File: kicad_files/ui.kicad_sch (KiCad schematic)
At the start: 0 parts

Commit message: UI schematic and external connectors
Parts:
- added Q2: NPN, symbol Simulation_SPICE:NPN
- added Q3: NMOS, symbol Simulation_SPICE:NMOS
- added R10, R11, R12: 10k, symbol Device:R_US
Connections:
- new net: Q2.2 (B), Q3.1 (D), R10.2
- new net: Q3.2 (G), R12.1
- new net 5V: R10.1, R11.1
- new net 5V PWM: Q2.3 (E), R11.2
- new net MCU PWM: R12.2
- new net gnd: Q2.1 (C), Q3.3 (S)

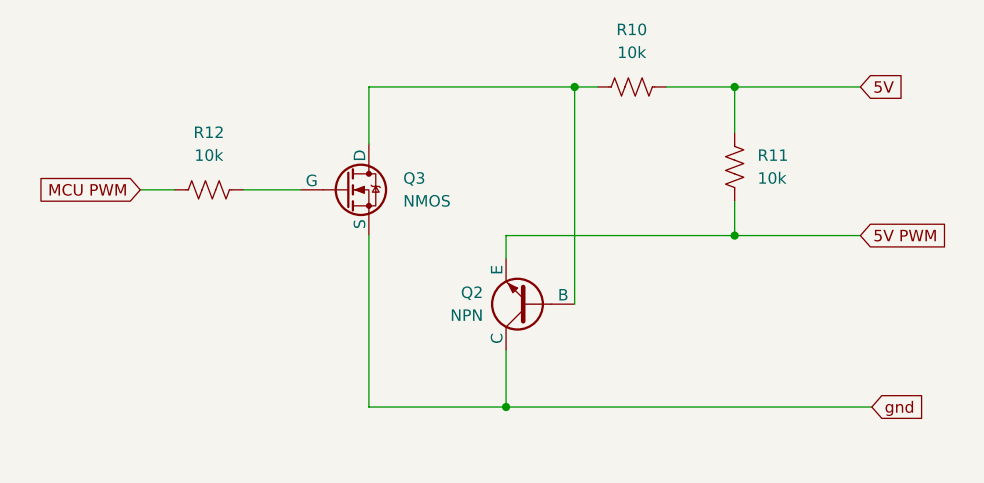
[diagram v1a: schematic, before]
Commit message: Hierarchical labels finished. Flyback diode issue fixed. I2C pins added
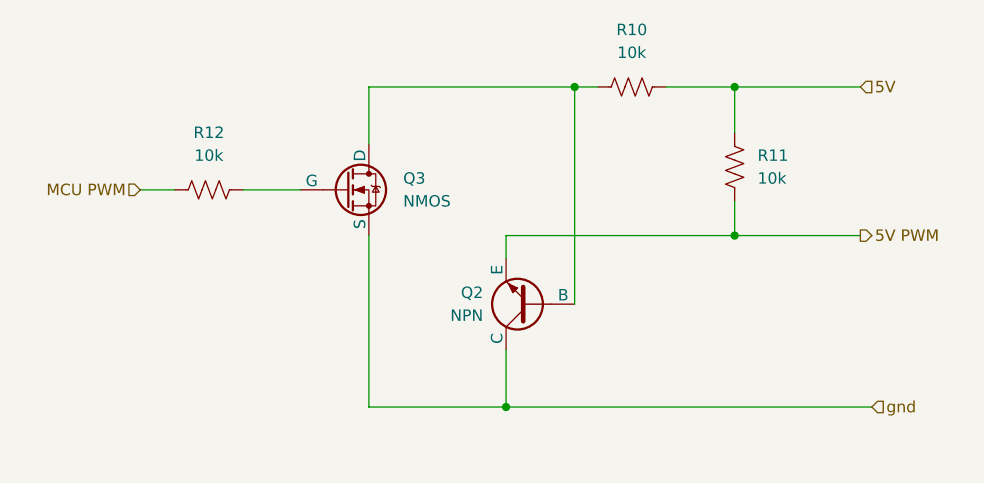
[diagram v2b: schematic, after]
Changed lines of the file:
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@@
 		)
 	)
-	(global_label "5V PWM"
+	(hierarchical_label "gnd"
 		(shape input)
-		(at 177.8 97.79 0)
-		(fields_autoplaced yes)
+		(at 179.07 116.84 0)
 		(effects
 			(font
@@
 			(justify left)
 		)
-		(property "Intersheetrefs" "${INTERSHEET_REFS}"
-			(at 188.2237 97.79 0)
-			(effects
-				(font
-					(size 1.27 1.27)
-				)
-				(justify left)
-				(hide yes)
+	)
+	(hierarchical_label "MCU PWM"
+		(shape input)
+		(at 97.79 92.71 180)
+		(effects
+			(font
+				(size 1.27 1.27)
 			)
+			(justify right)
 		)
 	)
-	(global_label "5V"
-		(shape input)
-		(at 177.8 81.28 0)
-		(fields_autoplaced yes)
+	(hierarchical_label "5V PWM"
+		(shape output)
+		(at 177.8 97.79 0)
 		(effects
 			(font
@@
 			(justify left)
 		)
-		(property "Intersheetrefs" "${INTERSHEET_REFS}"
-			(at 183.0833 81.28 0)
-			(effects
-				(font
-					(size 1.27 1.27)
-				)
-				(justify left)
-				(hide yes)
-			)
-		)
 	)
-	(global_label "MCU PWM"
+	(hierarchical_label "5V"
 		(shape input)
-		(at 97.79 92.71 180)
-		(fields_autoplaced yes)
-		(effects
-			(font
-				(size 1.27 1.27)
-			)
-			(justify right)
-		)
-		(property "Intersheetrefs" "${INTERSHEET_REFS}"
-			(at 85.6125 92.71 0)
-			(effects
-				(font
-					(size 1.27 1.27)
-				)
-				(justify right)
-				(hide yes)
-			)
-		)
-	)
-	(global_label "gnd"
-		(shape input)
-		(at 179.07 116.84 0)
-		(fields_autoplaced yes)
+		(at 177.8 81.28 0)
 		(effects
 			(font
@@
 			(justify left)
 		)
-		(property "Intersheetrefs" "${INTERSHEET_REFS}"
-			(at 185.5022 116.84 0)
-			(effects
-				(font
-					(size 1.27 1.27)
-				)
-				(justify left)
-				(hide yes)
-			)
-		)
 	)

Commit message: ERC errors cleaned. Hierarchical wiring finished. PWM converter change. Motor driver change.
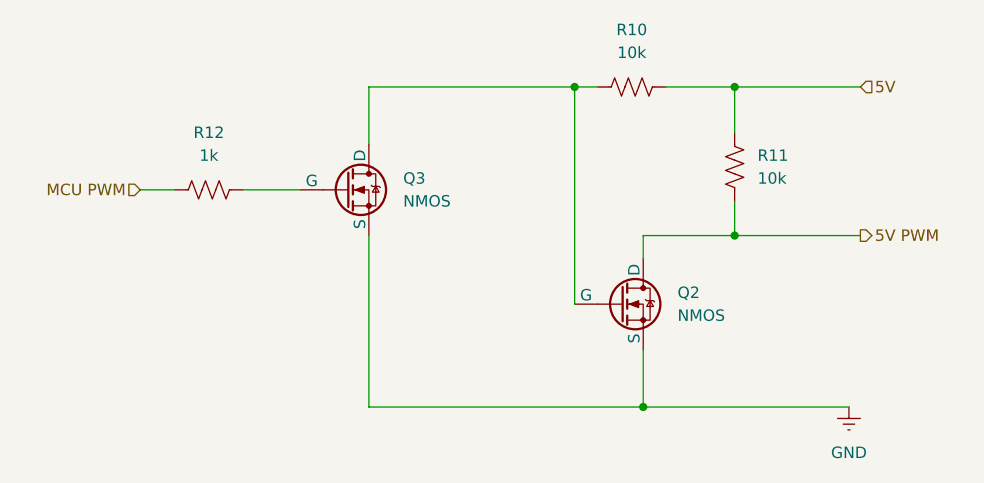
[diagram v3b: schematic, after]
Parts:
- removed Q2: NPN, symbol Simulation_SPICE:NPN
- added Q2: NMOS, symbol Simulation_SPICE:NMOS
- R12: value 10k -> 1k
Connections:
- net 5V PWM: now also Q2.1 (D)
- net at Q3.1 (D), R10.2: now also Q2.2 (G)
- net gnd renamed GND
- net GND: now also Q2.3 (S)
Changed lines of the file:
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@@
 	)
 	(junction
-		(at 138.43 116.84)
+		(at 153.67 116.84)
 		(diameter 0)
 		(color 0 0 0 0)
@@
 	(wire
 		(pts
-			(xy 138.43 110.49) (xy 138.43 116.84)
+			(xy 153.67 110.49) (xy 153.67 116.84)
 		)
 		(stroke
@@
 	(wire
 		(pts
-			(xy 138.43 116.84) (xy 179.07 116.84)
-		)
-		(stroke
-			(width 0)
-			(type default)
-		)
-	)
-	(wire
-		(pts
-			(xy 123.19 116.84) (xy 138.43 116.84)
+			(xy 123.19 116.84) (xy 153.67 116.84)
 		)
 		(stroke
@@
 	(wire
 		(pts
+			(xy 153.67 116.84) (xy 176.53 116.84)
+		)
+		(stroke
+			(width 0)
+			(type default)
+		)
+	)
+	(wire
+		(pts
 			(xy 123.19 81.28) (xy 123.19 87.63)
 		)
@@
 	(wire
 		(pts
-			(xy 138.43 97.79) (xy 138.43 100.33)
+			(xy 153.67 97.79) (xy 153.67 100.33)
 		)
 		(stroke
@@
 	(wire
 		(pts
-			(xy 163.83 97.79) (xy 138.43 97.79)
+			(xy 163.83 97.79) (xy 153.67 97.79)
 		)
 		(stroke
@@
 			(width 0)
 			(type default)
-		)
-	)
-	(hierarchical_label "gnd"
-		(shape input)
-		(at 179.07 116.84 0)
-		(effects
-			(font
-				(size 1.27 1.27)
-			)
-			(justify left)
 		)
 	)
@@
 			)
 			(justify left)
+		)
+	)
+	(symbol
+		(lib_id "Simulation_SPICE:NMOS")
+		(at 151.13 105.41 0)
+		(unit 1)
+		(exclude_from_sim no)
+		(in_bom yes)
+		(on_board yes)
+		(dnp no)
+		(fields_autoplaced yes)
+		(property "Reference" "Q2"
+			(at 157.48 104.1399 0)
+			(effects
+				(font
+					(size 1.27 1.27)
+				)
+				(justify left)
+			)
+		)
+		(property "Value" "NMOS"
+			(at 157.48 106.6799 0)
+			(effects
+				(font
+					(size 1.27 1.27)
+				)
+				(justify left)
+			)
+		)
+		(property "Footprint" ""
+			(at 156.21 102.87 0)
+			(effects
+				(font
+					(size 1.27 1.27)
+				)
+				(hide yes)
+			)
+		)
+		(property "Datasheet" "https://ngspice.sourceforge.io/docs/ngspice-html-manual/manual.xhtml#cha_MOSFETs"
+			(at 151.13 118.11 0)
+			(effects
+				(font
+					(size 1.27 1.27)
+				)
+				(hide yes)
+			)
+		)
+		(property "Description" "N-MOSFET transistor, drain/source/gate"
+			(at 151.13 105.41 0)
+			(effects
+				(font
+					(size 1.27 1.27)
+				)
+				(hide yes)
+			)
+		)
+		(property "Sim.Device" "NMOS"
+			(at 151.13 122.555 0)
+			(effects
+				(font
+					(size 1.27 1.27)
+				)
+				(hide yes)
+			)
+		)
+		(property "Sim.Type" "VDMOS"
+			(at 151.13 124.46 0)
+			(effects
+				(font
+					(size 1.27 1.27)
+				)
+				(hide yes)
+			)
+		)
+		(property "Sim.Pins" "1=D 2=G 3=S"
+			(at 151.13 120.65 0)
+			(effects
+				(font
+					(size 1.27 1.27)
+				)
+				(hide yes)
+			)
+		)
+		(pin "2"
+		)
+		(pin "3"
+		)
+		(pin "1"
+		)
+		(instances
+			(project "kicad_files"
+				(path "/67de3bec-6c8a-4e66-9cf7-9a8a92865209/ce830c06-a9b3-40f6-b6fa-b8cd2779ee31"
+					(reference "Q2")
+					(unit 1)
+				)
+			)
+		)
+	)
+	(symbol
+		(lib_id "power:GNDREF")
+		(at 176.53 116.84 0)
+		(unit 1)
+		(exclude_from_sim no)
+		(in_bom yes)
+		(on_board yes)
+		(dnp no)
+		(fields_autoplaced yes)
+		(property "Reference" "#PWR010"
+			(at 176.53 123.19 0)
+			(effects
+				(font
+					(size 1.27 1.27)
+				)
+				(hide yes)
+			)
+		)
+		(property "Value" "GND"
+			(at 176.53 121.92 0)
+			(effects
+				(font
+					(size 1.27 1.27)
+				)
+			)
+		)
+		(property "Footprint" ""
+			(at 176.53 116.84 0)
+			(effects
+				(font
+					(size 1.27 1.27)
+				)
+				(hide yes)
+			)
+		)
+		(property "Datasheet" ""
+			(at 176.53 116.84 0)
+			(effects
+				(font
+					(size 1.27 1.27)
+				)
+				(hide yes)
+			)
+		)
+		(property "Description" "Power symbol creates a global label with name \"GNDREF\" , reference supply ground"
+			(at 176.53 116.84 0)
+			(effects
+				(font
+					(size 1.27 1.27)
+				)
+				(hide yes)
+			)
+		)
+		(pin "1"
+		)
+		(instances
+			(project "kicad_files"
+				(path "/67de3bec-6c8a-4e66-9cf7-9a8a92865209/ce830c06-a9b3-40f6-b6fa-b8cd2779ee31"
+					(reference "#PWR010")
+					(unit 1)
+				)
+			)
 		)
 	)
@@
 			)
 		)
-		(property "Value" "10k"
+		(property "Value" "1k"
 			(at 105.41 88.9 90)
 			(effects
@@
 					(unit 1)
 				)
-			)
-		)
-	)
-	(symbol
-		(lib_id "Simulation_SPICE:NPN")
-		(at 140.97 105.41 180)
-		(unit 1)
-		(exclude_from_sim no)
-		(in_bom yes)
-		(on_board yes)
-		(dnp no)
-		(fields_autoplaced yes)
-		(property "Reference" "Q2"
-			(at 135.89 104.1399 0)
-			(effects
-				(font
-					(size 1.27 1.27)
-				)
-				(justify left)
-			)
-		)
-		(property "Value" "NPN"
-			(at 135.89 106.6799 0)
-			(effects
-				(font
-					(size 1.27 1.27)
-				)
-				(justify left)
-			)
-		)
-		(property "Footprint" ""
-			(at 77.47 105.41 0)
-			(effects
-				(font
-					(size 1.27 1.27)
-				)
-				(hide yes)
-			)
-		)
-		(property "Datasheet" "https://ngspice.sourceforge.io/docs/ngspice-html-manual/manual.xhtml#cha_BJTs"
-			(at 77.47 105.41 0)
-			(effects
-				(font
-					(size 1.27 1.27)
-				)
-				(hide yes)
-			)
-		)
-		(property "Description" "Bipolar transistor symbol for simulation only, substrate tied to the emitter"
-			(at 140.97 105.41 0)
-			(effects
-				(font
-					(size 1.27 1.27)
-				)
-				(hide yes)
-			)
-		)
-		(property "Sim.Device" "NPN"
-			(at 140.97 105.41 0)
-			(effects
-				(font
-					(size 1.27 1.27)
-				)
-				(hide yes)
-			)
-		)
-		(property "Sim.Type" "GUMMELPOON"
-			(at 140.97 105.41 0)
-			(effects
-				(font
-					(size 1.27 1.27)
-				)
-				(hide yes)
-			)
-		)
-		(property "Sim.Pins" "1=C 2=B 3=E"
-			(at 140.97 105.41 0)
-			(effects
-				(font
-					(size 1.27 1.27)
-				)
-				(hide yes)
-			)
-		)
-		(pin "3"
-		)
-		(pin "1"
-		)
-		(pin "2"
-		)
-		(instances
-			(project ""
-				(path "/67de3bec-6c8a-4e66-9cf7-9a8a92865209/ce830c06-a9b3-40f6-b6fa-b8cd2779ee31"
-					(reference "Q2")
-					(unit 1)
-				)

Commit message: Footprint assignment finished
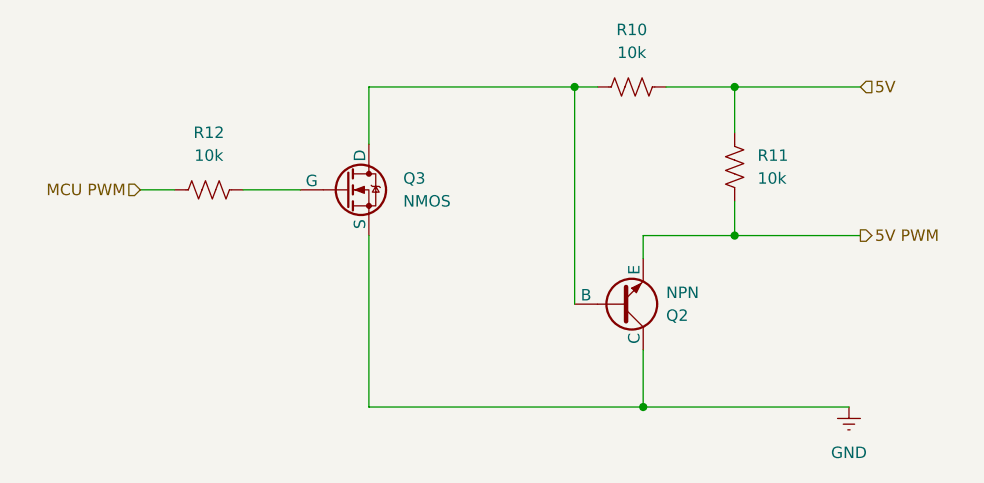
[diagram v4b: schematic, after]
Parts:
- Q2: value NMOS -> NPN; footprint (none) -> Package_TO_SOT_SMD:TSOT-23; symbol Simulation_SPICE:NMOS -> Simulation_SPICE:NPN
- Q3: footprint (none) -> Package_TO_SOT_SMD:SOT-323_SC-70
- R10, R11: footprint (none) -> Resistor_SMD:R_1206_3216Metric_Pad1.30x1.75mm_HandSolder
- R12: value 1k -> 10k; footprint (none) -> Resistor_SMD:R_1206_3216Metric_Pad1.30x1.75mm_HandSolder
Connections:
- net 5V PWM: now also Q2.3 (E); no longer Q2.1 (D)
- net GND: now also Q2.1 (C); no longer Q2.3 (S)
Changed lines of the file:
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@@
 	)
 	(symbol
-		(lib_id "Simulation_SPICE:NMOS")
+		(lib_id "Simulation_SPICE:NPN")
 		(at 151.13 105.41 0)
-		(unit 1)
-		(exclude_from_sim no)
-		(in_bom yes)
-		(on_board yes)
-		(dnp no)
-		(fields_autoplaced yes)
+		(mirror x)
+		(unit 1)
+		(exclude_from_sim no)
+		(in_bom yes)
+		(on_board yes)
+		(dnp no)
 		(property "Reference" "Q2"
-			(at 157.48 104.1399 0)
-			(effects
-				(font
-					(size 1.27 1.27)
-				)
-				(justify left)
-			)
-		)
-		(property "Value" "NMOS"
-			(at 157.48 106.6799 0)
-			(effects
-				(font
-					(size 1.27 1.27)
-				)
-				(justify left)
-			)
-		)
-		(property "Footprint" ""
-			(at 156.21 102.87 0)
-			(effects
-				(font
-					(size 1.27 1.27)
-				)
-				(hide yes)
-			)
-		)
-		(property "Datasheet" "https://ngspice.sourceforge.io/docs/ngspice-html-manual/manual.xhtml#cha_MOSFETs"
-			(at 151.13 118.11 0)
-			(effects
-				(font
-					(size 1.27 1.27)
-				)
-				(hide yes)
-			)
-		)
-		(property "Description" "N-MOSFET transistor, drain/source/gate"
+			(at 156.21 106.6801 0)
+			(effects
+				(font
+					(size 1.27 1.27)
+				)
+				(justify left)
+			)
+		)
+		(property "Value" "NPN"
+			(at 156.21 104.1401 0)
+			(effects
+				(font
+					(size 1.27 1.27)
+				)
+				(justify left)
+			)
+		)
+		(property "Footprint" "Package_TO_SOT_SMD:TSOT-23"
+			(at 214.63 105.41 0)
+			(effects
+				(font
+					(size 1.27 1.27)
+				)
+				(hide yes)
+			)
+		)
+		(property "Datasheet" "https://ngspice.sourceforge.io/docs/ngspice-html-manual/manual.xhtml#cha_BJTs"
+			(at 214.63 105.41 0)
+			(effects
+				(font
+					(size 1.27 1.27)
+				)
+				(hide yes)
+			)
+		)
+		(property "Description" "Bipolar transistor symbol for simulation only, substrate tied to the emitter"
 			(at 151.13 105.41 0)
 			(effects
@@
 			)
 		)
-		(property "Sim.Device" "NMOS"
-			(at 151.13 122.555 0)
-			(effects
-				(font
-					(size 1.27 1.27)
-				)
-				(hide yes)
-			)
-		)
-		(property "Sim.Type" "VDMOS"
-			(at 151.13 124.46 0)
-			(effects
-				(font
-					(size 1.27 1.27)
-				)
-				(hide yes)
-			)
-		)
-		(property "Sim.Pins" "1=D 2=G 3=S"
-			(at 151.13 120.65 0)
+		(property "Sim.Device" "NPN"
+			(at 151.13 105.41 0)
+			(effects
+				(font
+					(size 1.27 1.27)
+				)
+				(hide yes)
+			)
+		)
+		(property "Sim.Type" "GUMMELPOON"
+			(at 151.13 105.41 0)
+			(effects
+				(font
+					(size 1.27 1.27)
+				)
+				(hide yes)
+			)
+		)
+		(property "Sim.Pins" "1=C 2=B 3=E"
+			(at 151.13 105.41 0)
 			(effects
 				(font
@@
 			)
 		)
-		(property "Footprint" ""
+		(property "Footprint" "Resistor_SMD:R_1206_3216Metric_Pad1.30x1.75mm_HandSolder"
 			(at 152.146 82.296 90)
 			(effects
@@
 			)
 		)
-		(property "Value" "1k"
+		(property "Value" "10k"
 			(at 105.41 88.9 90)
 			(effects
@@
 			)
 		)
-		(property "Footprint" ""
+		(property "Footprint" "Resistor_SMD:R_1206_3216Metric_Pad1.30x1.75mm_HandSolder"
 			(at 105.156 93.726 90)
 			(effects
@@
 			)
 		)
-		(property "Footprint" ""
+		(property "Footprint" "Resistor_SMD:R_1206_3216Metric_Pad1.30x1.75mm_HandSolder"
 			(at 164.846 90.424 90)
 			(effects
@@
 			)
 		)
-		(property "Footprint" ""
+		(property "Footprint" "Package_TO_SOT_SMD:SOT-323_SC-70"
 			(at 125.73 90.17 0)
 			(effects
